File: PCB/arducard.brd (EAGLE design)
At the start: 100 x 80 mm, 92 parts, among them J1 USB MICRO, Q1 BC817-16LT1SMD, Q2 DMG2301U-7, Q3 2N7002, Q4 BSS84, Q5 2N7002, Q6 2N7002, Q7 2N7002, Q8 BSS84, Q9 DMG2301U-7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

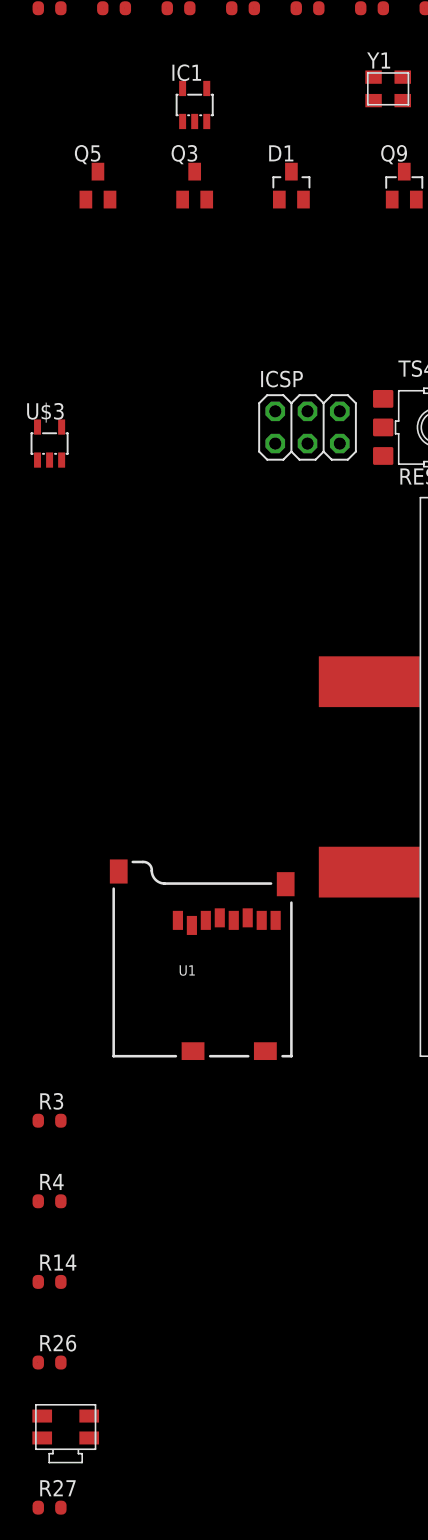
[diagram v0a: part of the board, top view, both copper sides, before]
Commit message: added 5th button
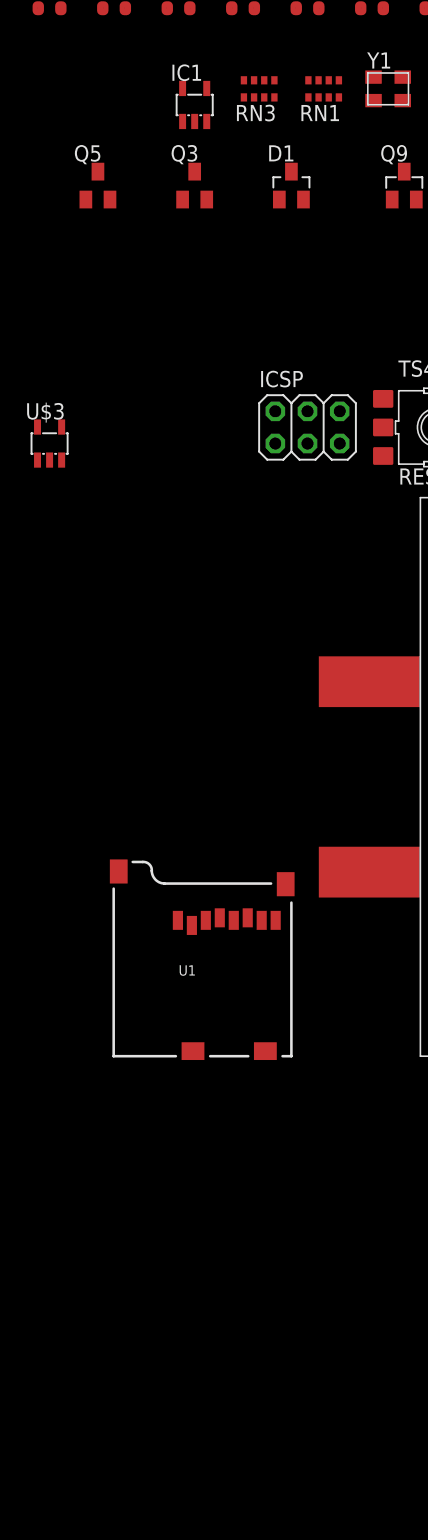
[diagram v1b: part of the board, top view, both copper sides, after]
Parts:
- removed R14, R4: 22R, SmartPrj:R0603-ROUND
- removed R26: 150, SmartPrj:R0603-ROUND
- removed R27, R3: 10k, SmartPrj:R0603-ROUND
- removed U$1: EVQ-PUA, arducard-switch:SMD-TACT-SWITCH
- added RN1: 10K, resistor-dil:CAY16
- added RN3: 22R, resistor-dil:CAY16
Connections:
- removed net B4: R26.1, U2.12
- removed net N$8: R26.2, R27.1, U$1.1, U$1.3
- removed net RTC_INT: R19.1, U2.30, U4.5
- removed net SD_CD: R13.2, U2.29
- new net CD: R13.2, U2.8
- new net N$17: R19.1, U4.5
- net +3V3: now also R10.2, R12.2, R6.2, R8.2, RN1.5; no longer R3.2, U$1.2, U$1.4, U$11.2, U$11.4, U$14.2, U$14.4, U$8.2, U$8.4, U$9.2, U$9.4
- net D+: now also RN3.8; no longer R4.1
- net D-: now also RN3.5; no longer R14.1
- net EPD_CS: no longer U2.27
- net FRAM_CS: now also U2.28; no longer U2.25
- net GND: now also U$11.2, U$11.4, U$14.2, U$14.4, U$8.2, U$8.4, U$9.2, U$9.4; no longer R10.2, R12.2, R27.2, R6.2, R8.2
- net RD+: now also RN3.1; no longer R4.2
- net RD-: now also RN3.4; no longer R14.2
- net RESET: now also RN1.4; no longer R3.1
- net RTC_CS: no longer U2.26
- net SD_CS: now also U2.29; no longer U2.22
